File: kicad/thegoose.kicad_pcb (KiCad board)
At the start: 4 copper layers, 60 x 50 mm, 40 parts, among them U1 DRV8848, U2 DRV8848, U3 DRV8848, U4 AP64500SP-13

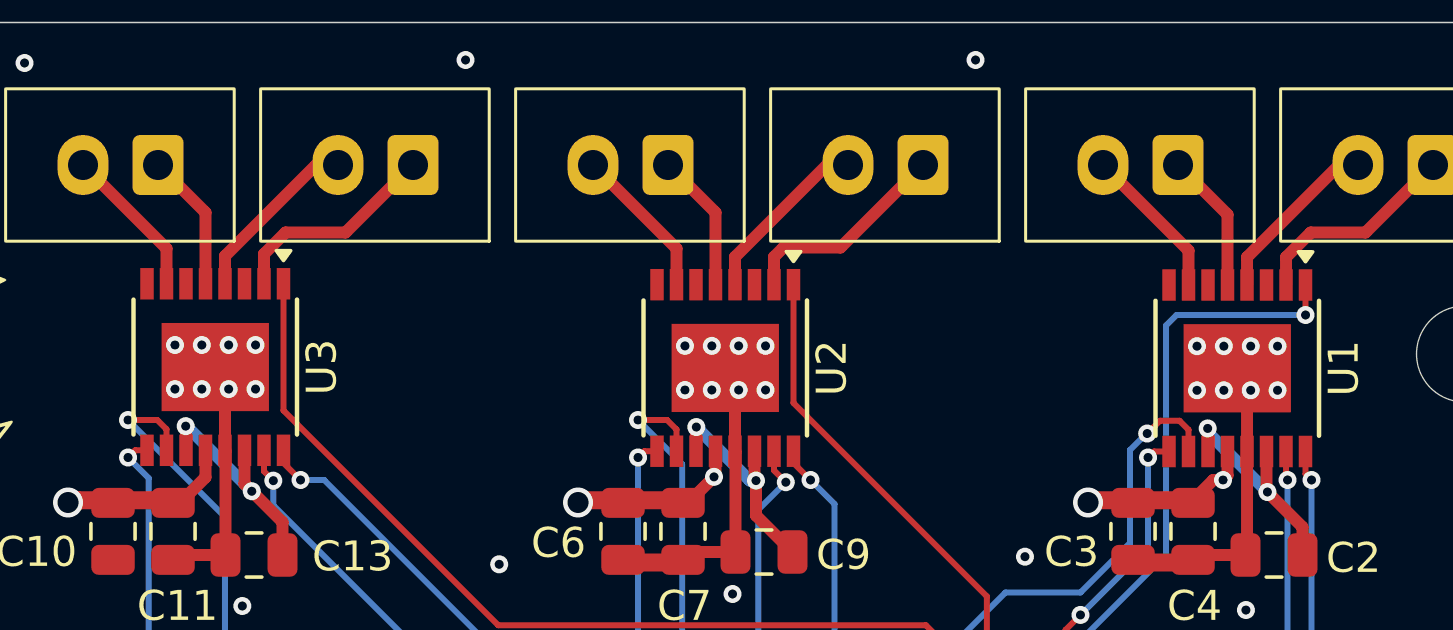
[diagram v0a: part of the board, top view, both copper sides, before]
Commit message: Tie DRV8848 sense pins to GND
AISEN and BISEN on U1-U3 were left open, so the H-bridges' low side had
no return path. Without current limiting, the data sheet says to tie
them to GND. Done in the SKiDL source, the schematic and the PCB (short
tracks from each pad to GND).

The PCB file is now saved in KiCad 10 format, which accounts for most of
its diff.

Co-Authored-By: Claude Opus 5.5 <noreply@anthropic.com>
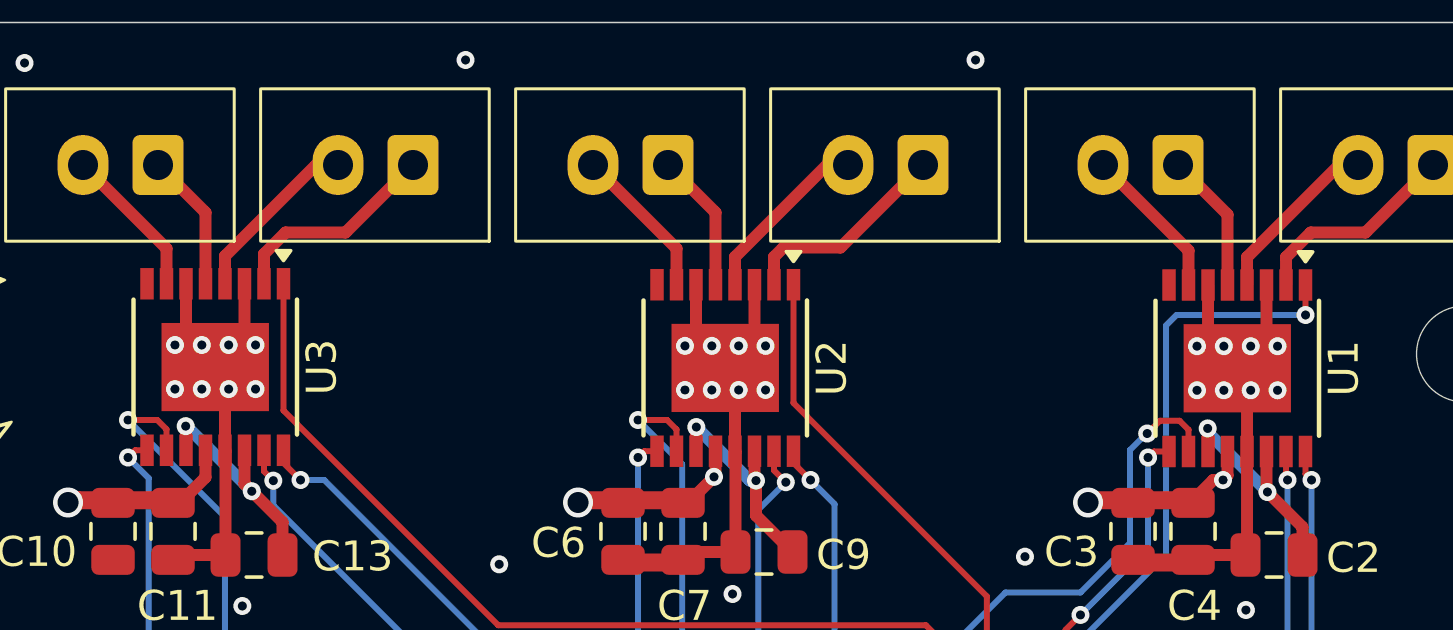
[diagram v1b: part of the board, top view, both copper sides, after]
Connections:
- U1 pad 3: unconnected-(U1-AISEN-Pad3) -> GND
- U1 pad 6: unconnected-(U1-BISEN-Pad6) -> GND
- U2 pad 3: unconnected-(U2-AISEN-Pad3) -> GND
- U2 pad 6: unconnected-(U2-BISEN-Pad6) -> GND
- U3 pad 3: unconnected-(U3-AISEN-Pad3) -> GND
- U3 pad 6: unconnected-(U3-BISEN-Pad6) -> GND
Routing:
- net GND: track 41.2 -> 53.4 mm

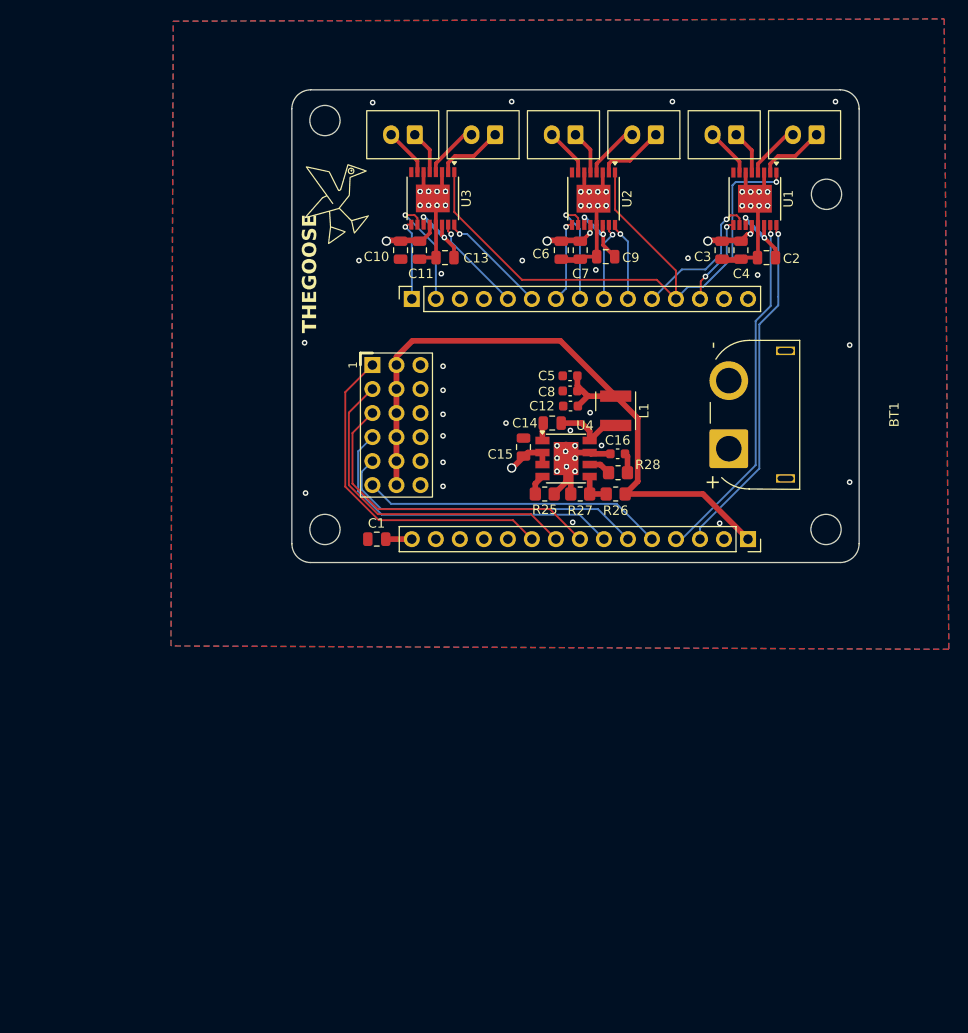
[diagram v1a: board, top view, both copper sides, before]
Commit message: Lay out rev 2 with an internal pack, protector and cost-down parts
Board is 91 x 47 mm for a 96 x 52 mm enclosure, with placement and hand
power routing done; signal routing is still to do.

- Internal Gens Ace 3S 1000 mAh pack on an XT60 pigtail, protected on the
  board by a BQ7791501 with back-to-back low-side FETs and a 2.5 mOhm
  shunt, plus a balance header and two NTCs.
- USB-A and USB-C on the top edge, IO as a recessed 3 x 6 pin block, GPIO
  map re-swapped for the placement, USB nets renamed with P/N suffixes
  for the diff-pair router.
- Cost-down swaps that keep every feature: basic or preferred passives
  and ICs, cheaper connectors, a THT power switch rated for 12.6 V, and
  replacements for the low-stock TH1 and Q2/Q3. L3 is Digi-Key sourced
  and hand-placed.
- Net classes and design rules, rev 2 power-net widths in review.py, and
  the PCB critic and loop updated for rev 2.

Schematic review passes; PCB review passes every gate except unrouted.

Co-Authored-By: Claude Opus 5.5 <noreply@anthropic.com>
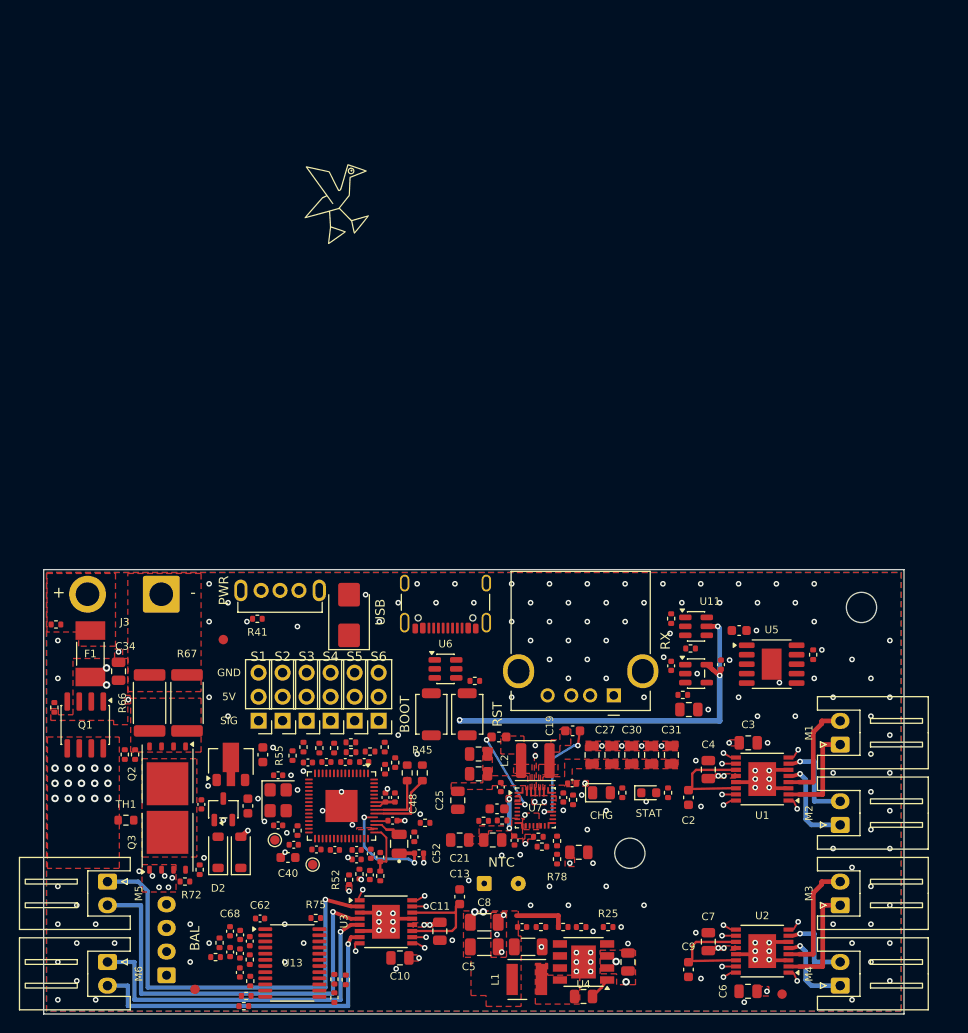
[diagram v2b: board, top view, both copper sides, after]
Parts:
- removed BT1: XT60, hexy:AMASS_XT60PW-M_1x02_P7.20mm_Horizontal
- removed C1: 1uF, Capacitor_SMD:C_0805_2012Metric
- removed ESP32_1, ESP32_2: Conn_01x15_Socket, Connector_PinSocket_2.54mm:PinSocket_1x15_P2.54mm_Vertical
- removed GPIO1: Conn_06x3_Pin, hexy:PinHeader_3x06_P2.54mm_Horizontal
- removed the REF** at (182.8, 60.3)
- removed the REF** at (182.8, 95.8)
- removed the REF** at (129.8, 95.8)
- removed the REF** at (129.8, 52.5)
- added C17: 1uF, Capacitor_SMD:C_0603_1608Metric, F.Cu at (173.6, 106.4)
- added C18: 47nF, Capacitor_SMD:C_0603_1608Metric, F.Cu at (148.2, 117.7)
- added C19: 47nF, Capacitor_SMD:C_0603_1608Metric, F.Cu at (155.9, 117.0)
- added C20: 10uF, Capacitor_SMD:C_0805_2012Metric, F.Cu at (147.5, 128.6)
- added C21: 10uF, Capacitor_SMD:C_0805_2012Metric, F.Cu at (144.0, 128.6)
- added C22: 100nF, Capacitor_SMD:C_0402_1005Metric, F.Cu at (149.8, 128.7)
- added C23: 10uF, Capacitor_SMD:C_0805_2012Metric, F.Cu at (146.0, 121.6)
- added C24: 10uF, Capacitor_SMD:C_0805_2012Metric, F.Cu at (146.0, 119.5)
- added C25: 10uF, Capacitor_SMD:C_0805_2012Metric, F.Cu at (143.8, 124.4)
- added C26: 100nF, Capacitor_SMD:C_0402_1005Metric, F.Cu at (148.3, 123.0)
- added C27: 10uF, Capacitor_SMD:C_0805_2012Metric, F.Cu at (160.1, 119.6)
- added C28: 10uF, Capacitor_SMD:C_0805_2012Metric, F.Cu at (164.3, 119.6)
- added C29: 10uF, Capacitor_SMD:C_0805_2012Metric, F.Cu at (158.0, 119.6)
- added C30: 10uF, Capacitor_SMD:C_0805_2012Metric, F.Cu at (162.2, 119.6)
- added C31: 10uF, Capacitor_SMD:C_0805_2012Metric, F.Cu at (166.4, 119.6)
- added C32: 100nF, Capacitor_SMD:C_0402_1005Metric, F.Cu at (155.9, 122.6)
- added C33: 10uF, Capacitor_SMD:C_0805_2012Metric, F.Cu at (156.6, 129.9)
- added C34: 10uF, Capacitor_SMD:C_0805_2012Metric, F.Cu at (107.9, 110.8)
- added C35: 4.7uF, Capacitor_SMD:C_0603_1608Metric, F.Cu at (147.9, 125.3)
- added C36: 1nF, Capacitor_SMD:C_0402_1005Metric, F.Cu at (155.0, 124.1)
- added C37: 1uF, Capacitor_SMD:C_0603_1608Metric, F.Cu at (123.2, 119.6)
- added C38: 10uF, Capacitor_SMD:C_0603_1608Metric, F.Cu at (121.6, 125.0)
- added C39: 1uF, Capacitor_SMD:C_0402_1005Metric, F.Cu at (116.7, 124.8)
- added C40: 10uF, Capacitor_SMD:C_0603_1608Metric, F.Cu at (125.8, 130.4)
- added C41: 100nF, Capacitor_SMD:C_0402_1005Metric, F.Cu at (133.9, 120.3)
- added C42: 100nF, Capacitor_SMD:C_0402_1005Metric, F.Cu at (129.9, 120.3)
- added C43: 100nF, Capacitor_SMD:C_0402_1005Metric, F.Cu at (128.0, 120.4)
- added C44: 100nF, Capacitor_SMD:C_0402_1005Metric, F.Cu at (126.5, 129.1)
- added C45: 100nF, Capacitor_SMD:C_0402_1005Metric, F.Cu at (133.1, 129.7)
- added C46: 100nF, Capacitor_SMD:C_0402_1005Metric, F.Cu at (134.6, 130.1)
- added C47: 100nF, Capacitor_SMD:C_0402_1005Metric, F.Cu at (136.2, 124.1)
- added C48: 100nF, Capacitor_SMD:C_0402_1005Metric, F.Cu at (137.2, 124.1)
- added C49: 100nF, Capacitor_SMD:C_0402_1005Metric, F.Cu at (133.1, 130.7)
- added C50: 4.7uF, Capacitor_SMD:C_0402_1005Metric, F.Cu at (136.9, 126.5)
- added C51: 4.7uF, Capacitor_SMD:C_0402_1005Metric, F.Cu at (135.6, 130.4)
- added C52: 4.7uF, Capacitor_SMD:C_0402_1005Metric, F.Cu at (139.7, 130.0)
- added C53: 100nF, Capacitor_SMD:C_0402_1005Metric, F.Cu at (131.9, 120.3)
- added C54: 100nF, Capacitor_SMD:C_0402_1005Metric, F.Cu at (128.8, 129.6)
- added C55: 100nF, Capacitor_SMD:C_0402_1005Metric, F.Cu at (130.8, 129.7)
- added C56: 15pF, Capacitor_SMD:C_0402_1005Metric, F.Cu at (124.8, 121.8)
- added C57: 15pF, Capacitor_SMD:C_0402_1005Metric, F.Cu at (124.8, 127.0)
- added C58: 1uF, Capacitor_SMD:C_0402_1005Metric, F.Cu at (171.6, 110.0)
- added C59: 10uF, Capacitor_SMD:C_0805_2012Metric, F.Cu at (168.2, 114.8)
- added C60: 100nF, Capacitor_SMD:C_0402_1005Metric, F.Cu at (166.4, 110.2)
- added C61: 100nF, Capacitor_SMD:C_0402_1005Metric, F.Cu at (134.5, 132.3)
- added C62: 1uF, Capacitor_SMD:C_0402_1005Metric, F.Cu at (122.9, 136.9)
- added C63: 1uF, Capacitor_SMD:C_0402_1005Metric, F.Cu at (121.8, 139.3)
- added C64: 1uF, Capacitor_SMD:C_0402_1005Metric, F.Cu at (119.7, 140.4)
- added C65: 1uF, Capacitor_SMD:C_0402_1005Metric, F.Cu at (120.8, 142.6)
- added C66: 1uF, Capacitor_SMD:C_0402_1005Metric, F.Cu at (120.8, 140.6)
- added C67: 1uF, Capacitor_SMD:C_0402_1005Metric, F.Cu at (120.8, 138.6)
- added C68: 100nF, Capacitor_SMD:C_0402_1005Metric, F.Cu at (119.7, 138.2)
- added D1: SMBJ20A, Diode_SMD:D_SMB, F.Cu at (132.3, 104.8)
- added D2: B5819W, Diode_SMD:D_SOD-123, F.Cu at (118.5, 129.9)
- added D3: B5819W, Diode_SMD:D_SOD-123, F.Cu at (120.8, 129.9)
- added F1: 15A fast, Fuse:Fuse_Littelfuse-NANO2-451_453, F.Cu at (104.9, 108.9)
- added FID1: Fiducial, Fiducial:Fiducial_1mm_Mask2mm, F.Cu at (116.0, 144.4)
- added FID2: Fiducial, Fiducial:Fiducial_1mm_Mask2mm, F.Cu at (178.1, 144.9)
- added FID3: Fiducial, Fiducial:Fiducial_1mm_Mask2mm, F.Cu at (119.0, 107.4)
- added J1: USB_C_Receptacle_USB2.0_16P, hexy:USB_C_Receptacle_ShouHan_TYPE-C16PIN, F.Cu at (142.5, 102.5)
- added J10: IO6, Connector_PinHeader_2.54mm:PinHeader_1x03_P2.54mm_Vertical, F.Cu at (135.4, 116.0)
- added J11: Balance, Connector_JST:JST_XH_B4B-XH-A_1x04_P2.50mm_Vertical, B.Cu at (113.0, 142.9)
- added J2: NTC bead 10k B3435, Connector_Wire:SolderWire-0.1sqmm_1x02_P3.6mm_D0.4mm_OD1mm, F.Cu at (146.6, 133.2)
- added J3: XT60-F pigtail 14AWG, Connector_Wire:SolderWire-2sqmm_1x02_P7.8mm_D2mm_OD3.9mm, F.Cu at (112.4, 102.6)
- added J4: USB-A host, hexy:USB_A_ShouHan_AF90_WJDG, F.Cu at (160.3, 113.3)
- added J5: IO1, Connector_PinHeader_2.54mm:PinHeader_1x03_P2.54mm_Vertical, F.Cu at (122.7, 116.0)
- added J6: IO2, Connector_PinHeader_2.54mm:PinHeader_1x03_P2.54mm_Vertical, F.Cu at (125.3, 116.0)
- added J7: IO3, Connector_PinHeader_2.54mm:PinHeader_1x03_P2.54mm_Vertical, F.Cu at (127.8, 116.0)
- added J8: IO4, Connector_PinHeader_2.54mm:PinHeader_1x03_P2.54mm_Vertical, F.Cu at (130.3, 116.0)
- added J9: IO5, Connector_PinHeader_2.54mm:PinHeader_1x03_P2.54mm_Vertical, F.Cu at (132.9, 116.0)
- added L2: 2.2uH, Inductor_SMD:L_Changjiang_FNR4030S, F.Cu at (152.0, 120.2)
- added L3: 3.3uH, hexy:L_Abracon_AOTA-B201610, F.Cu at (137.6, 129.0)
- added LED1: green, LED_SMD:LED_0805_2012Metric, F.Cu at (159.0, 123.6)
- added LED2: red, LED_SMD:LED_0603_1608Metric, F.Cu at (164.0, 123.6)
- added Q1: AO4407A, Package_SO:SOIC-8_3.9x4.9mm_P1.27mm, F.Cu at (104.4, 116.4)
- added Q2: 80N03F, Package_TO_SOT_SMD:TDSON-8-1, F.Cu at (113.1, 121.6)
- added Q3: 80N03F, Package_TO_SOT_SMD:TDSON-8-1, F.Cu at (113.1, 128.8)
- added R29: 6.8k, Resistor_SMD:R_0402_1005Metric, F.Cu at (181.4, 109.0)
- added R30: 100, Resistor_SMD:R_0402_1005Metric, F.Cu at (152.3, 128.3)
- added R31: 6.8k, Resistor_SMD:R_0402_1005Metric, F.Cu at (154.3, 128.7)
- added R32: 100k, Resistor_SMD:R_0402_1005Metric, F.Cu at (148.5, 126.5)
- added R33: 33k, Resistor_SMD:R_0402_1005Metric, F.Cu at (146.5, 126.6)
- added R34: 5.23k, Resistor_SMD:R_0402_1005Metric, F.Cu at (152.7, 129.3)
- added R35: 30.1k, Resistor_SMD:R_0402_1005Metric, F.Cu at (156.0, 124.3)
- added R36: 2.2k, Resistor_SMD:R_0402_1005Metric, F.Cu at (161.2, 123.6)
- added R37: 10k, Resistor_SMD:R_0402_1005Metric, F.Cu at (136.1, 121.1)
- added R38: 10k, Resistor_SMD:R_0402_1005Metric, F.Cu at (132.5, 119.3)
- added R39: 10k, Resistor_SMD:R_0402_1005Metric, F.Cu at (134.5, 119.2)
- added R40: 100k, Resistor_SMD:R_0402_1005Metric, F.Cu at (101.1, 114.6)
- added R41: 1k, Resistor_SMD:R_0402_1005Metric, F.Cu at (122.6, 105.2)
- added R42: 33, Resistor_SMD:R_0402_1005Metric, F.Cu at (135.6, 132.4)
- added R43: 1k, Resistor_SMD:R_0402_1005Metric, F.Cu at (126.8, 127.6)
- added R44: 27, Resistor_SMD:R_0603_1608Metric, F.Cu at (138.4, 121.5)
- added R45: 27, Resistor_SMD:R_0603_1608Metric, F.Cu at (140.1, 121.5)
- added R46: 1k, Resistor_SMD:R_0402_1005Metric, F.Cu at (137.2, 120.4)
- added R47: 1k, Resistor_SMD:R_0402_1005Metric, F.Cu at (145.6, 111.8)
- added R48: 22, Resistor_SMD:R_0402_1005Metric, F.Cu at (166.4, 105.2)
- added R49: 22, Resistor_SMD:R_0402_1005Metric, F.Cu at (168.4, 108.3)
- added R50: 100k, Resistor_SMD:R_0402_1005Metric, F.Cu at (140.3, 126.8)
- added R51: 1k, Resistor_SMD:R_0402_1005Metric, F.Cu at (166.0, 123.6)
- added R52: 100k, Resistor_SMD:R_0402_1005Metric, F.Cu at (132.3, 132.8)
- added R53: 27k, Resistor_SMD:R_0402_1005Metric, F.Cu at (133.4, 132.2)
- added R54: 10k, Resistor_SMD:R_0402_1005Metric, F.Cu at (139.2, 128.3)
- added R55: 330, Resistor_SMD:R_0402_1005Metric, F.Cu at (126.3, 119.7)
- added R56: 330, Resistor_SMD:R_0402_1005Metric, F.Cu at (127.5, 118.8)
- added R57: 330, Resistor_SMD:R_0402_1005Metric, F.Cu at (129.2, 118.9)
- added R58: 330, Resistor_SMD:R_0402_1005Metric, F.Cu at (130.7, 118.9)
- added R59: 330, Resistor_SMD:R_0402_1005Metric, F.Cu at (132.5, 118.3)
- added R60: 330, Resistor_SMD:R_0402_1005Metric, F.Cu at (136.1, 118.8)
- added R61: 1k, Resistor_SMD:R_0402_1005Metric, F.Cu at (101.3, 105.8)
- added R62: 100, Resistor_SMD:R_0402_1005Metric, F.Cu at (121.2, 146.2)
- added R63: 100, Resistor_SMD:R_0402_1005Metric, F.Cu at (121.4, 145.1)
- added R64: 100, Resistor_SMD:R_0402_1005Metric, F.Cu at (121.8, 143.5)
- added R65: 100, Resistor_SMD:R_0402_1005Metric, F.Cu at (121.8, 141.2)
- added R66: 5m, Resistor_SMD:R_2512_6332Metric, F.Cu at (111.2, 114.1)
- added R67: 5m, Resistor_SMD:R_2512_6332Metric, F.Cu at (115.2, 114.1)
- added R68: 100, Resistor_SMD:R_0402_1005Metric, F.Cu at (118.2, 141.0)
- added R69: 100, Resistor_SMD:R_0402_1005Metric, F.Cu at (118.6, 139.5)
- added R70: 4.7k, Resistor_SMD:R_0402_1005Metric, F.Cu at (109.7, 119.6)
- added R71: 1M, Resistor_SMD:R_0402_1005Metric, F.Cu at (108.6, 119.6)
- added R72: 1k, Resistor_SMD:R_0402_1005Metric, F.Cu at (114.9, 133.0)
- added R73: 1M, Resistor_SMD:R_0402_1005Metric, F.Cu at (116.5, 131.7)
- added R74: 470k, Resistor_SMD:R_0402_1005Metric, F.Cu at (130.8, 145.3)
- added R75: 10k, Resistor_SMD:R_0402_1005Metric, F.Cu at (128.8, 136.8)
- added R76: 100k, Resistor_SMD:R_0402_1005Metric, F.Cu at (130.8, 143.3)
- added R77: 10k, Resistor_SMD:R_0402_1005Metric, F.Cu at (131.9, 143.4)
- added R78: 6.8k, Resistor_SMD:R_0402_1005Metric, F.Cu at (154.3, 130.6)
- added R79: 10k, Resistor_SMD:R_0402_1005Metric, F.Cu at (167.6, 113.2)
- added REF**: MountingHole_3.2mm, MountingHole:MountingHole_3.2mm_M3, F.Cu at (186.5, 104.0)
- added REF**: MountingHole_3.2mm, MountingHole:MountingHole_3.2mm_M3, F.Cu at (162.0, 130.0)
- added SW1: Power, hexy:SW_SPDT_ShouHan_SK12D07VG4, F.Cu at (125.0, 102.2)
- added SW2: BOOT, Button_Switch_SMD:SW_SPST_TS-1088-xR020, F.Cu at (141.0, 115.3)
- added SW3: RESET, Button_Switch_SMD:SW_SPST_TS-1088-xR020, F.Cu at (144.8, 115.3)
- added TH1: 10k B3434, Resistor_SMD:R_0603_1608Metric, F.Cu at (108.7, 126.5)
- added TP1: SWCLK, TestPoint:TestPoint_Pad_D1.0mm, F.Cu at (124.5, 128.6)
- added TP2: SWDIO, TestPoint:TestPoint_Pad_D1.0mm, F.Cu at (128.4, 131.2)
- added U10: RP2354A, Package_DFN_QFN:QFN-60-1EP_7x7mm_P0.4mm_EP3.4x3.4mm, F.Cu at (131.5, 125.0)
- added U11: SRV05-4, Package_TO_SOT_SMD:SOT-23-6, F.Cu at (169.0, 106.0)
- added U12: SY6280AAC, Package_TO_SOT_SMD:SOT-23-5, F.Cu at (169.0, 111.0)
- added U13: BQ7791501, Package_SO:TSSOP-24_4.4x7.8mm_P0.65mm, F.Cu at (126.3, 141.6)
- added U5: CH224A, Package_SO:SSOP-10-1EP_3.9x4.9mm_P1mm_EP2.1x3.3mm, F.Cu at (177.0, 110.0)
- added U6: SRV05-4, Package_TO_SOT_SMD:SOT-23-6, F.Cu at (142.5, 110.5)
- added U7: BQ25798, Package_DFN_QFN:Texas_RQM0029A_VQFN-29_4x4mm_P0.4mm, F.Cu at (152.0, 125.2)
- added U8: HT7550-1, Package_TO_SOT_SMD:SOT-89-3, F.Cu at (119.8, 120.3)
- added U9: XC6206P332MR, Package_TO_SOT_SMD:SOT-23-3, F.Cu at (119.0, 125.3)
- added Y1: 12MHz, Crystal:Crystal_SMD_3225-4Pin_3.2x2.5mm, F.Cu at (124.8, 124.4)
- C12, C5, C8: footprint Capacitor_SMD:C_0603_1608Metric -> Capacitor_SMD:C_1206_3216Metric
- C13, C2, C9: footprint Capacitor_SMD:C_0805_2012Metric -> Capacitor_SMD:C_0603_1608Metric
- C16: value 2.7nF -> 4.7nF; footprint Capacitor_SMD:C_0603_1608Metric -> Capacitor_SMD:C_0402_1005Metric
- M1, M2, M3, M4, M5, M6: footprint hexy:JST_XH_S2B-XH-A_1x02_P2.50mm_Horizontal -> Connector_JST:JST_XH_S2B-XH-A_1x02_P2.50mm_Horizontal
- R25: footprint Resistor_SMD:R_0805_2012Metric_Pad1.20x1.40mm_HandSolder -> Resistor_SMD:R_0402_1005Metric
- R26: value 115k -> 39k; footprint Resistor_SMD:R_0805_2012Metric_Pad1.20x1.40mm_HandSolder -> Resistor_SMD:R_0402_1005Metric
- R27: value 22.1k -> 7.5k; footprint Resistor_SMD:R_0805_2012Metric_Pad1.20x1.40mm_HandSolder -> Resistor_SMD:R_0402_1005Metric
- R28: value 15.8k -> 15k; footprint Resistor_SMD:R_0805_2012Metric_Pad1.20x1.40mm_HandSolder -> Resistor_SMD:R_0402_1005Metric
- moved M4 94.3 mm to (184.2, 144.0), turned to 90 degrees
- moved M6 93.3 mm to (106.8, 141.5), turned to -90 degrees
- moved M5 89.0 mm to (106.8, 133.0), turned to -90 degrees
- moved M3 83.8 mm to (184.2, 135.5), turned to 90 degrees
- moved U2 81.6 mm to (176.0, 140.3), turned to 180 degrees
- moved C6 80.8 mm to (174.5, 144.6), turned to 0 degrees
- moved U3 76.7 mm to (136.2, 137.2), turned to 0 degrees
- moved C9 75.9 mm to (168.2, 142.3), turned to -90 degrees
- moved C10 74.9 mm to (137.7, 141.1), turned to 0 degrees
- moved C7 74.4 mm to (170.3, 139.3), turned to 90 degrees
- moved M2 73.8 mm to (184.2, 127.0), turned to 90 degrees
- moved C11 72.2 mm to (141.9, 138.2)
- moved C13 67.6 mm to (144.0, 134.6), turned to 90 degrees
- moved M1 64.5 mm to (184.2, 118.5), turned to 90 degrees
- moved U1 61.4 mm to (176.0, 122.2), turned to 180 degrees
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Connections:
- net +BATT renamed VSYS
- net /ESP_D2 renamed DRV_SLEEP
- net Net-(U1-VINT) renamed /Motor drivers/U1_VINT
- net Net-(U2-VINT) renamed /Motor drivers/U2_VINT
- net Net-(U3-VINT) renamed /Motor drivers/U3_VINT
- U1 pad 10: /ESP_D4 -> GPIO0_M2B
- U1 pad 15: /ESP_D12 -> GPIO11_M1B
- U1 pad 16: /ESP_D13 -> GPIO10_M1A
- U1 pad 8: unconnected-(U1-~{FAULT}-Pad8) -> DRV_FAULT
- U1 pad 9: /ESP_D15 -> GPIO1_M2A
- U2 pad 10: /ESP_D5 -> GPIO4_M4B
- U2 pad 15: /ESP_D17 -> GPIO19_M3B
- U2 pad 16: /ESP_D16 -> GPIO18_M3A
- U2 pad 8: unconnected-(U2-~{FAULT}-Pad8) -> DRV_FAULT
- U2 pad 9: /ESP_D18 -> GPIO5_M4A
- U3 pad 10: /ESP_D22 -> GPIO22_M6B
- U3 pad 15: /ESP_D21 -> GPIO25_M5B
- U3 pad 16: /ESP_D19 -> GPIO24_M5A
- U3 pad 8: unconnected-(U3-~{FAULT}-Pad8) -> DRV_FAULT
- U3 pad 9: /ESP_D23 -> GPIO23_M6A
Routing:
- net DRV_SLEEP: track 68.8 -> 3.16 mm, vias 1 -> 3
- net Net-(M5-OUT1): track 7.19 -> 45.2 mm, vias 0 -> 1
- net /ESP_D12: track 37.7 -> 0.00 mm, vias 1 -> 0
- net Net-(M5-OUT2): track 5.95 -> 43.3 mm, vias 0 -> 1
- net /ESP_D13: track 36.7 -> 0.00 mm, vias 1 -> 0
- net /ESP_D32: track 36.1 -> 0.00 mm
- net GND: track 53.4 -> 17.6 mm, vias 58 -> 191
- net /ESP_D33: track 35.5 -> 0.00 mm
- net /ESP_D25: track 34.8 -> 0.00 mm
- net /ESP_D26: track 34.4 -> 0.00 mm
- net /ESP_D27: track 33.8 -> 0.00 mm
- net Net-(M6-OUT1): track 4.62 -> 36.6 mm, vias 0 -> 1
- net /ESP_D14: track 31.9 -> 0.00 mm
- net Net-(M6-OUT2): track 5.11 -> 34.3 mm, vias 0 -> 1
- net VCC: track 75.9 -> 47.9 mm, vias 0 -> 6
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- added copper zone on F.Cu, net /Power & charging/BAT_N
- added copper zone on F.Cu, net /Power & charging/CHG_SYS
- added copper zone on F.Cu, net /Power & charging/PACK+
- added copper zone on F.Cu, net /Power & charging/PROT_FET_D
- added copper zone on F.Cu, net /Power & charging/PROT_SNS
- added copper zone on In2.Cu, net GND
- added copper zone on F.Cu, net Net-(U4-SW)
- added copper zone on F.Cu, net Net-(U7-PMID)
- added copper zone on F.Cu, net Net-(U7-SW1)
- added copper zone on F.Cu, net Net-(U7-SW2)
- added copper zone on F.Cu, net VBAT
- added copper zone on In2.Cu, net VBAT
- added copper zone on F.Cu, net VBUS
- added copper zone on F.Cu, net VCC
- added copper zone on In2.Cu, net VCC
- added copper zone on F.Cu, net VSYS
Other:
- board size 60 x 50 mm -> 91 x 47 mm
- board text added: "+"
- board text added: "-"
- board text added: "5V"
- board text added: "BAL"
- board text added: "BOOT"
- board text added: "CHG"
- board text added: "GND"
- board text added: "NTC"
- board text added: "PACK ENVELOPE 74 x 36 x 20 mm (Gens Ace 3S 1000, nominal 71.5 x 35 x 17), 2 mm behind the board"
- board text added: "PWR"
- board text added: "RST"
- board text added: "RX"
- board text added: "S1"
- board text added: "S2"
- board text added: "S3"
- board text added: "S4"
- board text added: "S5"
- board text added: "S6"
- board text added: "SIG"
- board text added: "STAT"
- board text added: "USB"
- board text added: "XT60 MATED PAIR: STAND ON EDGE HERE"
- board text added: "XT60 PIGTAIL"
- board text added: "leads exit at x 117 into the strip: XT60 pigtail + mated plug, balance to J11"
- board text removed: "THEGOOSE"

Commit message: Add a header for an external WS2812B LED stick
J12 (JST-PH 3-pin) feeds an 8-LED WS2812B stick mounted on the case's
top edge near the USB ports. GPIO21 drives it through a 74AHCT1G125 so
the data line reaches the 5 V VIH, with a 330 ohm series resistor and
10 uF at the connector. Power comes from the switched 5 V rail; firmware
should cap brightness (about 0.5 A at full white).

Co-Authored-By: Claude Opus 5.5 <noreply@anthropic.com>
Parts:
- added C69: 100nF, Capacitor_SMD:C_0402_1005Metric, F.Cu at (170.5, 102.2)
- added C70: 10uF, Capacitor_SMD:C_0805_2012Metric, F.Cu at (172.2, 102.2)
- added J12: LED stick, Connector_JST:JST_PH_B3B-PH-K_1x03_P2.00mm_Vertical, F.Cu at (175.9, 102.2)
- added R80: 330, Resistor_SMD:R_0402_1005Metric, F.Cu at (177.0, 106.5)
- added U14: 74AHCT1G125, Package_TO_SOT_SMD:SOT-23-5, F.Cu at (167.4, 102.2)
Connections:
- U10 pad 33: unconnected-(U10-GPIO21-Pad33) -> LED_DIN
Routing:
- net VCC: track 47.9 -> 62.4 mm
- net GND: vias 191 -> 185
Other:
- board text added: "D"
- board text added: "G"
- board text added: "LED"
